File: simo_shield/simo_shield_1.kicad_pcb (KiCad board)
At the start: 2 copper layers, 64.6 x 82.5 mm, 5 parts, among them J2 VBAT, U1 YAAJ_BluePill_Part_Like_SWD_B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, U2 elemon_board, U3 flash_externa, U4 mpu6050

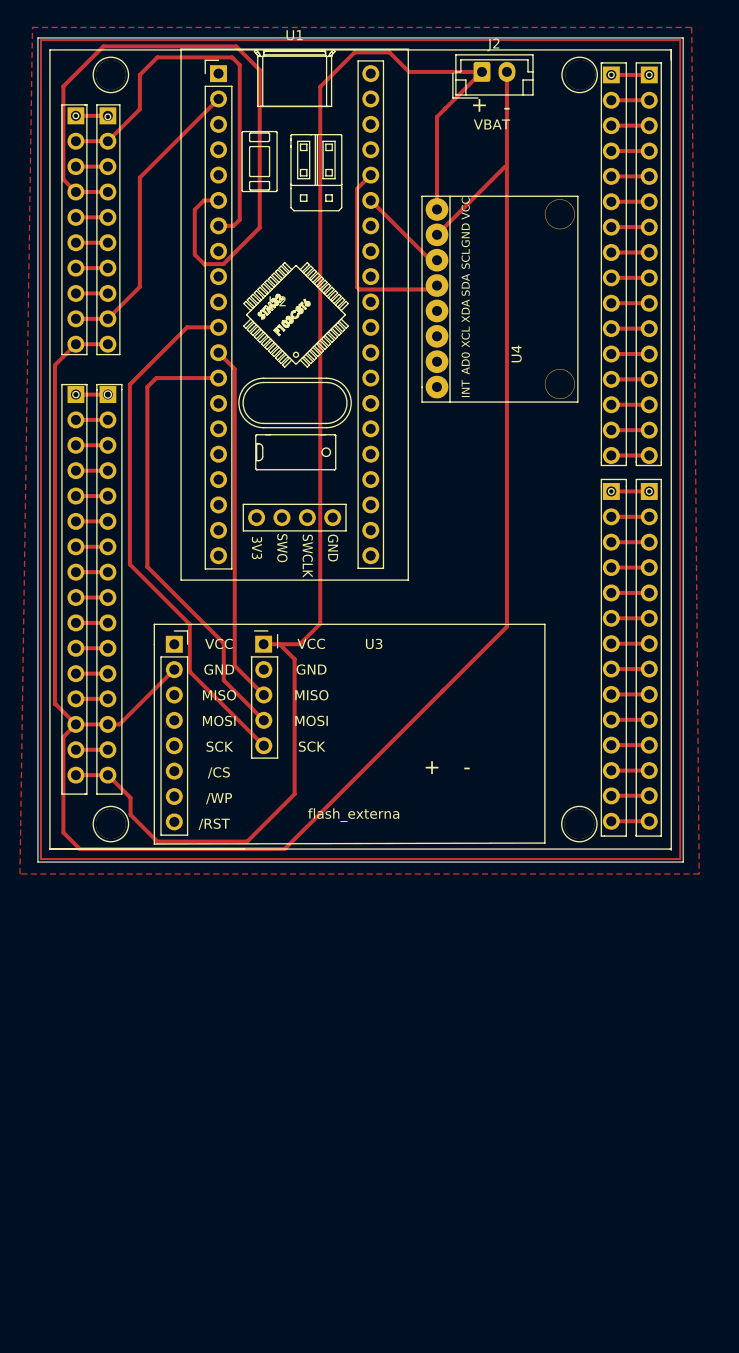
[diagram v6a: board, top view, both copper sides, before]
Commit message: verifique conexiones en simo shield, todo ok.
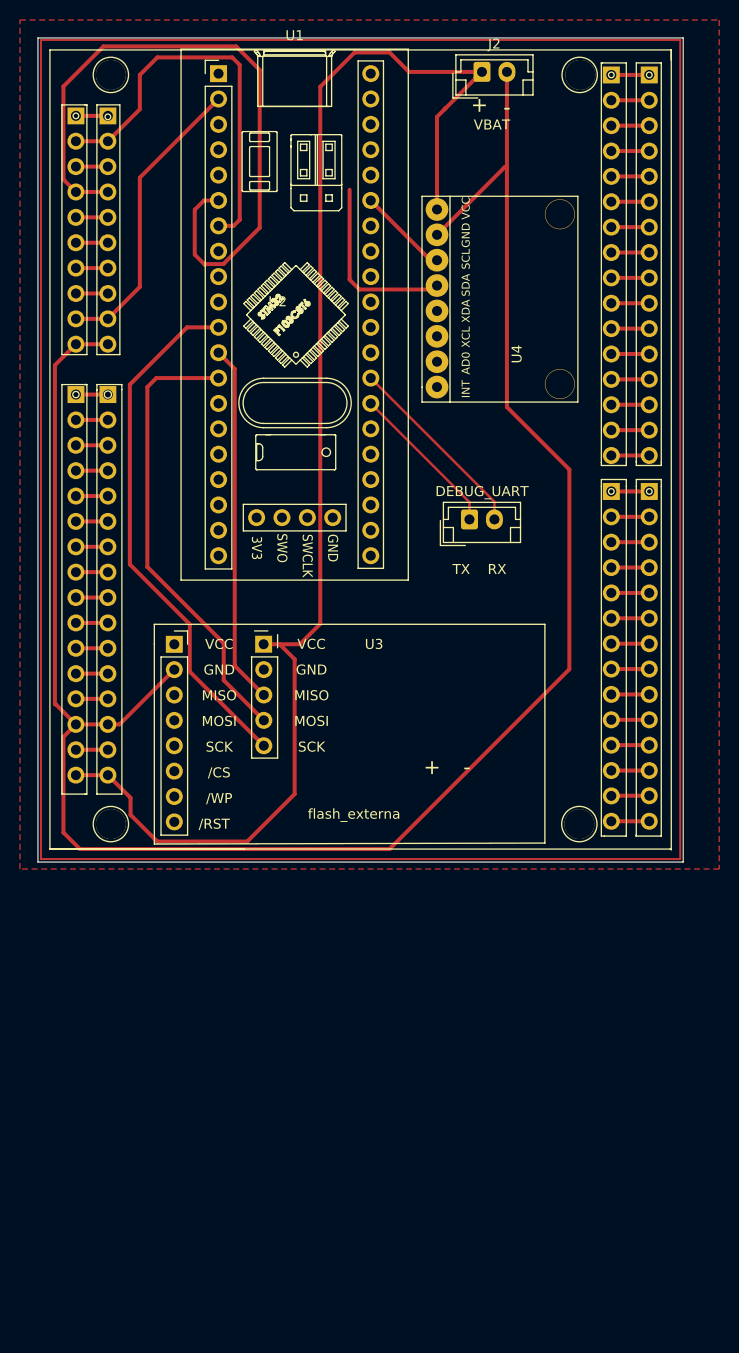
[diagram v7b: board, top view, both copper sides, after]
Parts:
- added DEBUG_UART: CONECTOR DEBUG_UART, Connector_JST:JST_EH_B2B-EH-A_1x02_P2.50mm_Vertical, F.Cu at (90.0, 115.0)
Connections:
- U1 pad 27: unconnected-(U1-Pad27) -> DEBUG_TX
- U1 pad 28: unconnected-(U1-Pad28) -> DEBUG_RX
- U2 pad 2: Net-(U1-Pad7) -> AT_RX
- U2 pad 4: Net-(U1-Pad6) -> AT_TX
- U2 pad 9: Net-(U1-Pad2) -> PWRUP
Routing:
- net Net-(U1-Pad6): track 68.1 -> 0.00 mm
- net AT_TX: track 0.00 -> 68.1 mm
- net Net-(U1-Pad7): track 40.1 -> 0.00 mm
- net AT_RX: track 0.00 -> 40.1 mm
- net PWRUP: track 0.00 -> 29.8 mm
- net Net-(U1-Pad2): track 29.8 -> 0.00 mm
- net DEBUG_RX: track 0.00 -> 19.3 mm
- net DEBUG_TX: track 0.00 -> 15.7 mm
- net GND_BAT: track 186.5 -> 197.5 mm
- net Net-(U1-Pad36): track 20.0 -> 18.3 mm

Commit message: en esquematico pin 35 y 36 se conectan con SDA y SCL de MPU6050. En PCB no aparece tal conexion
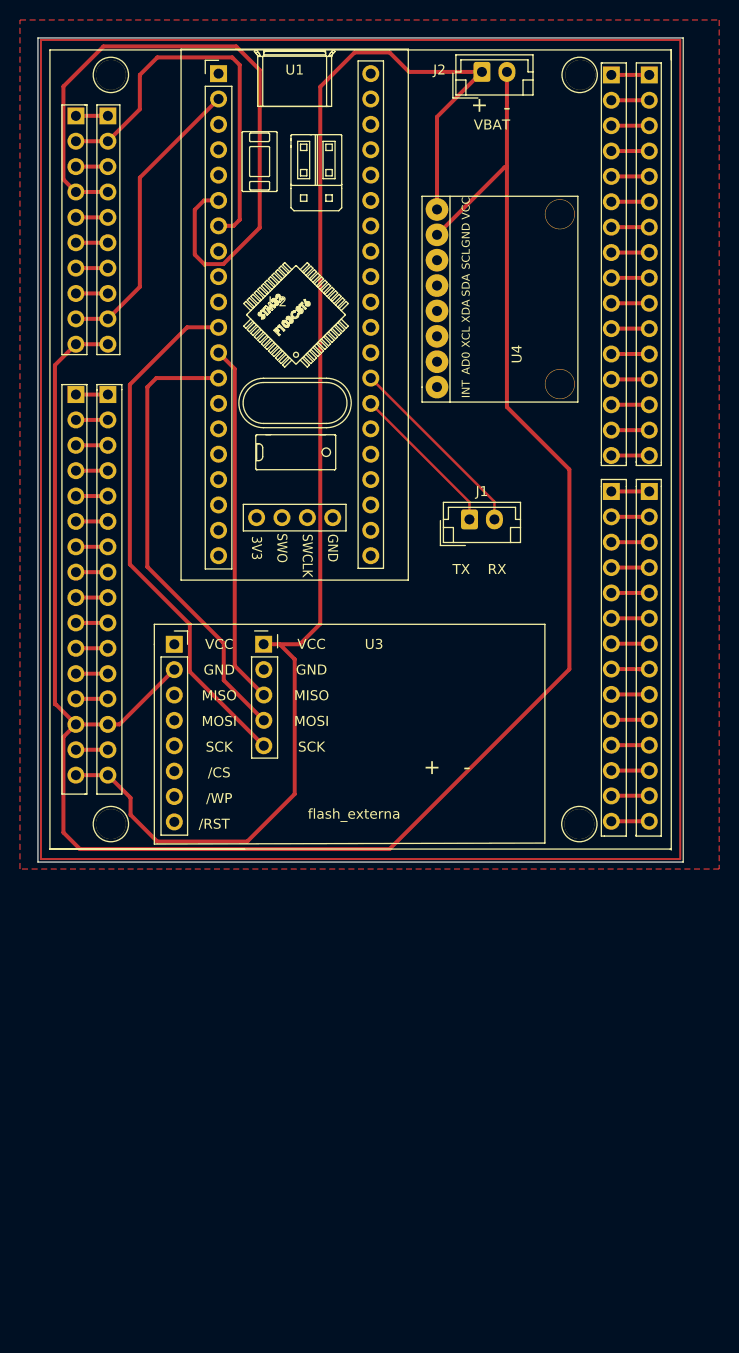
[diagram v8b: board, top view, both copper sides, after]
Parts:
- renumbered DEBUG_UART to J1
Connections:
- U4 pad 5: Net-(U1-Pad36) -> SCL_MPU6050
- U4 pad 6: Net-(U1-Pad35) -> SDA_MPU6050
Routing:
- net Net-(U1-Pad36): track 18.3 -> 0.00 mm
- net Net-(U1-Pad35): track 9.11 -> 0.00 mm
- net SCL_MPU6050: track 0.00 -> 0.55 mm
